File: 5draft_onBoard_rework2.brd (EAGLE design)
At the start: 100 x 82.5 mm, 69 parts, among them IC3 74ABT125PW, IC4 MAX4466KS, J2 USB_MINI-B_DIGIKEY, Q1 NPN 40V 1A SOT-23

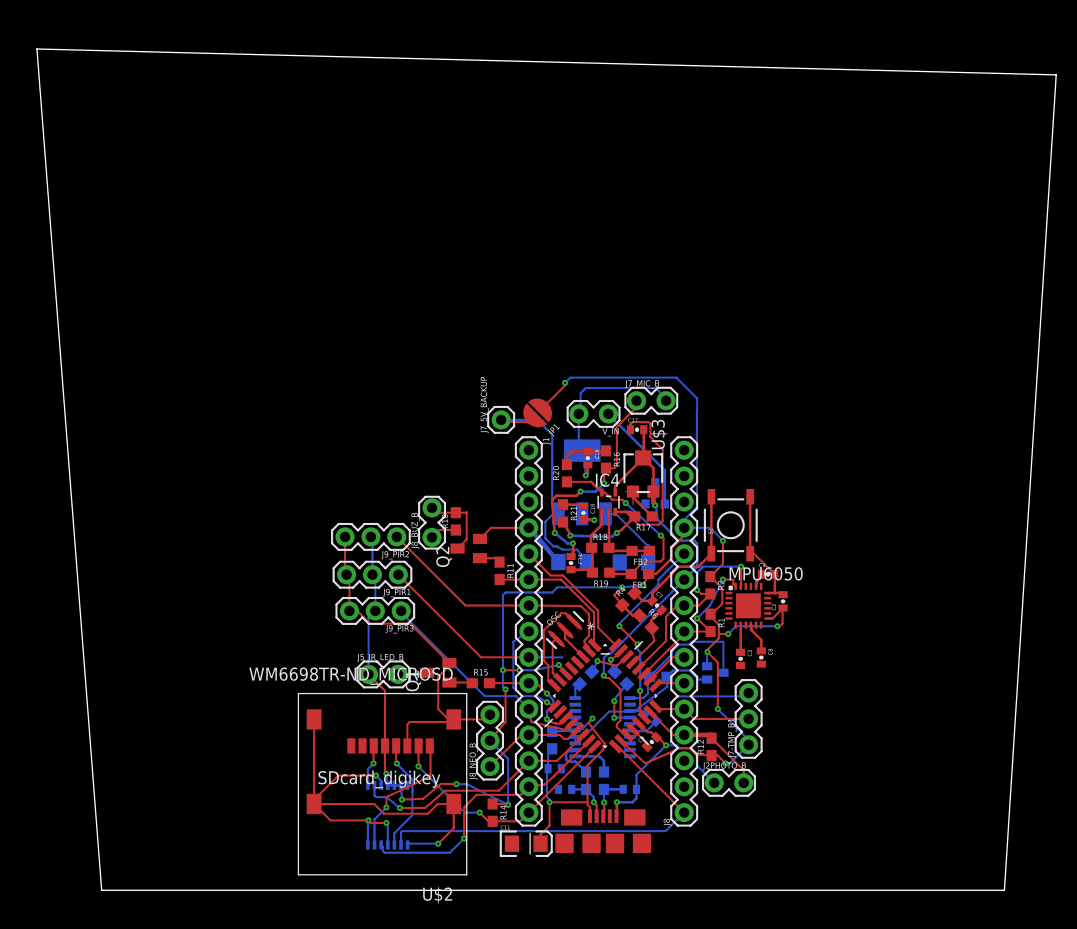
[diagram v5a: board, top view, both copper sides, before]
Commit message: routed, with pour. need to eddit quad buffer to be correct. Lots of DRC and ERC errors. Will start over
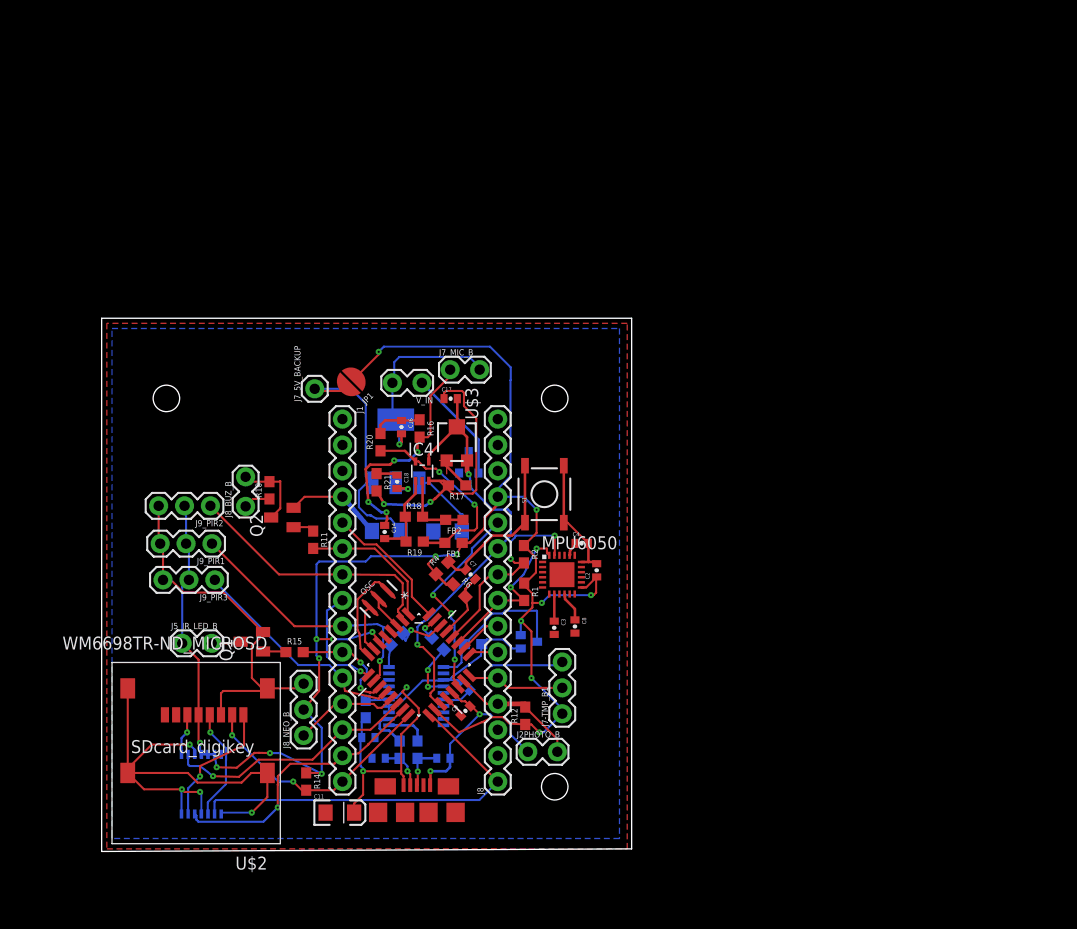
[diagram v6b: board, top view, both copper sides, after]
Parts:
- moved R8 18.9 mm to (29.0, 20.8)
- moved 5VREG 18.5 mm to (28.9, 39.3)
- moved C15 18.5 mm to (33.9, 31.4)
- moved C8 18.5 mm to (46.4, 22.1)
- moved FB1 18.5 mm to (34.5, 30.3)
- moved J5_IR_LED_B 18.5 mm to (8.08, 20.4)
- moved J8_BUZ_B 18.5 mm to (14.1, 34.0)
- moved Q1 18.5 mm to (14.7, 20.6)
- moved R6 18.5 mm to (35.1, 25.6)
- moved S1 18.5 mm to (43.4, 35.1)
- moved U$1 18.5 mm to (41.9, 20.6)
- moved U$3 18.5 mm to (34.8, 40.2)
- moved ATMEGA328P-AU 18.5 mm to (31.1, 18.3)
- moved C1 18.5 mm to (35.7, 16.3)
- moved C16 18.5 mm to (29.4, 41.6)
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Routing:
- net D6: track 19.5 -> 25.9 mm, vias 0 -> 1
- net RX-I: track 4.48 -> 5.38 mm
- net TX: track 1.94 -> 2.53 mm
- added copper zone on layer 1, net GND
- added copper zone on layer 16, net GND
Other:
- board size 100 x 82.5 mm -> 52 x 52.3 mm

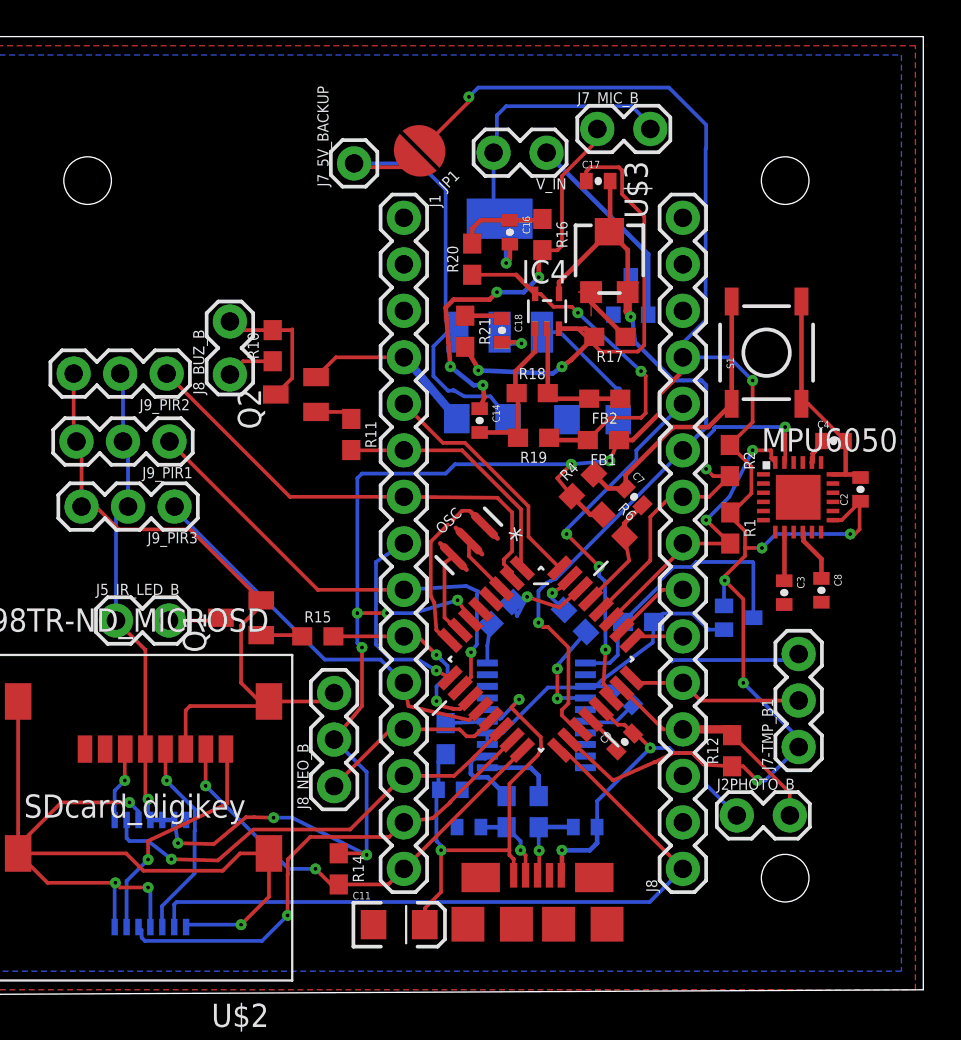
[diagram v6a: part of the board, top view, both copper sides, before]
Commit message: everything is added. IR fixed, beam break fixed. neo pixel added for fun this will be addressed at 1 and the one at top is addressed at 2
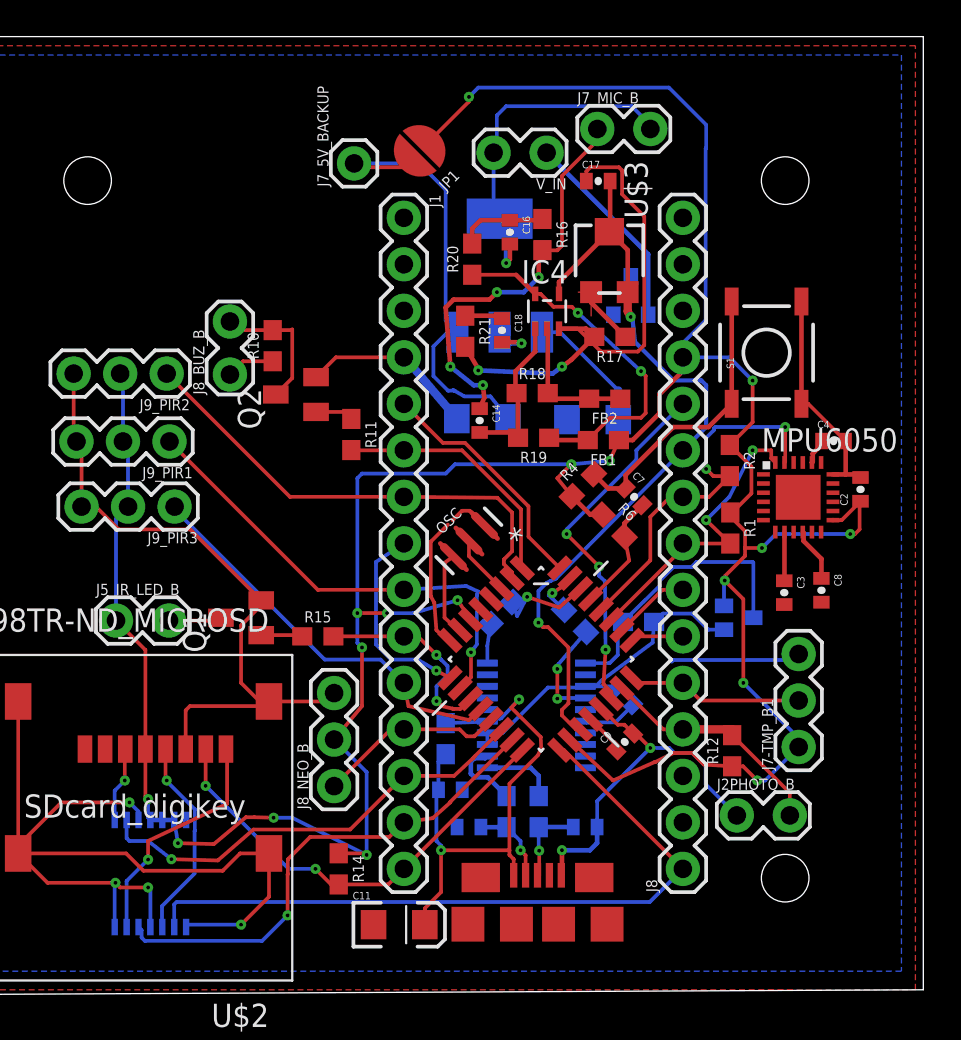
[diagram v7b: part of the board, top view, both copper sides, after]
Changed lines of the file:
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@@
 </class>
 </classes>
-<designrules name="advCircuits *">
+<designrules name="OSHPARKLaenPCBOrder">
 <description language="de">&lt;b&gt;EAGLE Design Rules&lt;/b&gt;
 &lt;p&gt;
@@
 Einstellungen hier und speichern die Design Rules unter
 einem neuen Namen ab.</description>
-<description language="en">&lt;b&gt;EAGLE Design Rules&lt;/b&gt;
+<description language="en">&lt;b&gt;Laen's PCB Order Design Rules&lt;/b&gt;
 &lt;p&gt;
-The default Design Rules have been set to cover
-a wide range of applications. Your particular design
-may have different requirements, so please make the
-necessary adjustments and save your customized
-design rules under a new name.</description>
+Please make sure your boards conform to these design rules.</description>
 <param name="layerSetup" value="(1*16)"/>
-<param name="mtCopper" value="0.035mm 0.035mm 0.035mm 0.035mm 0.035mm 0.035mm 0.035mm 0.035mm 0.035mm 0.035mm 0.035mm 0.035mm 0.035mm 0.035mm 0.035mm 0.035mm"/>
-<param name="mtIsolate" value="1.5mm 0.15mm 0.2mm 0.15mm 0.2mm 0.15mm 0.2mm 0.15mm 0.2mm 0.15mm 0.2mm 0.15mm 0.2mm 0.15mm 0.2mm"/>
-<param name="mdWireWire" value="8mil"/>
-<param name="mdWirePad" value="8mil"/>
-<param name="mdWireVia" value="8mil"/>
-<param name="mdPadPad" value="8mil"/>
-<param name="mdPadVia" value="8mil"/>
-<param name="mdViaVia" value="8mil"/>
-<param name="mdSmdPad" value="8mil"/>
-<param name="mdSmdVia" value="8mil"/>
-<param name="mdSmdSmd" value="8mil"/>
+<param name="mtCopper" value="0.0356mm 0.0356mm 0.0356mm 0.0356mm 0.0356mm 0.0356mm 0.0356mm 0.0356mm 0.0356mm 0.0356mm 0.0356mm 0.0356mm 0.0356mm 0.0356mm 0.0356mm 0.0356mm"/>
+<param name="mtIsolate" value="1.5011mm 0.1499mm 0.2007mm 0.1499mm 0.2007mm 0.1499mm 0.2007mm 0.1499mm 0.2007mm 0.1499mm 0.2007mm 0.1499mm 0.2007mm 0.1499mm 0.2007mm"/>
+<param name="mdWireWire" value="6mil"/>
+<param name="mdWirePad" value="6mil"/>
+<param name="mdWireVia" value="6mil"/>
+<param name="mdPadPad" value="6mil"/>
+<param name="mdPadVia" value="6mil"/>
+<param name="mdViaVia" value="6mil"/>
+<param name="mdSmdPad" value="6mil"/>
+<param name="mdSmdVia" value="6mil"/>
+<param name="mdSmdSmd" value="6mil"/>
 <param name="mdViaViaSameLayer" value="8mil"/>
 <param name="mnLayersViaInSmd" value="2"/>
-<param name="mdCopperDimension" value="40mil"/>
-<param name="mdDrill" value="8mil"/>
+<param name="mdCopperDimension" value="15mil"/>
+<param name="mdDrill" value="6mil"/>
 <param name="mdSmdStop" value="0mil"/>
-<param name="msWidth" value="8mil"/>
-<param name="msDrill" value="0.000203125mm"/>
-<param name="msMicroVia" value="0.000153125mm"/>
+<param name="msWidth" value="6mil"/>
+<param name="msDrill" value="13mil"/>
+<param name="msMicroVia" value="13mil"/>
 <param name="msBlindViaRatio" value="0.5"/>
 <param name="rvPadTop" value="0.25"/>
@@
 <param name="rvMicroViaOuter" value="0.25"/>
 <param name="rvMicroViaInner" value="0.25"/>
-<param name="rlMinPadTop" value="10mil"/>
+<param name="rlMinPadTop" value="7mil"/>
 <param name="rlMaxPadTop" value="20mil"/>
-<param name="rlMinPadInner" value="20mil"/>
+<param name="rlMinPadInner" value="7mil"/>
 <param name="rlMaxPadInner" value="20mil"/>
-<param name="rlMinPadBottom" value="10mil"/>
+<param name="rlMinPadBottom" value="7mil"/>
 <param name="rlMaxPadBottom" value="20mil"/>
-<param name="rlMinViaOuter" value="8mil"/>
-<param name="rlMaxViaOuter" value="10mil"/>
-<param name="rlMinViaInner" value="5mil"/>
-<param name="rlMaxViaInner" value="14mil"/>
+<param name="rlMinViaOuter" value="7mil"/>
+<param name="rlMaxViaOuter" value="20mil"/>
+<param name="rlMinViaInner" value="7mil"/>
+<param name="rlMaxViaInner" value="20mil"/>
 <param name="rlMinMicroViaOuter" value="4mil"/>
 <param name="rlMaxMicroViaOuter" value="20mil"/>
@@
 <param name="psTop" value="-1"/>
 <param name="psBottom" value="-1"/>
-<param name="psFirst" value="0"/>
+<param name="psFirst" value="-1"/>
 <param name="psElongationLong" value="100"/>
 <param name="psElongationOffset" value="100"/>
 <param name="mvStopFrame" value="1"/>
 <param name="mvCreamFrame" value="0"/>
-<param name="mlMinStopFrame" value="4mil"/>
-<param name="mlMaxStopFrame" value="4mil"/>
+<param name="mlMinStopFrame" value="3mil"/>
+<param name="mlMaxStopFrame" value="3mil"/>
 <param name="mlMinCreamFrame" value="0mil"/>
 <param name="mlMaxCreamFrame" value="0mil"/>
@@
 <param name="checkFont" value="1"/>
 <param name="checkRestrict" value="1"/>
-<param name="useDiameter" value="29"/>
+<param name="useDiameter" value="13"/>
 <param name="maxErrors" value="50"/>
 </designrules>
